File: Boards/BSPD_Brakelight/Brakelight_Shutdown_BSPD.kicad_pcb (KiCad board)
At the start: 2 copper layers, 91.4 x 66 mm, 85 parts, among them IC1 ATMEGA16M1, J2 MM_F_RA_20, J3 CONN_02X03, Q1 SSM3K333R, Q2 SSM3K333R, Q3 SSM3K333R, Q6 SSM3K333R, U1 SN74LVC1G08, U101 TPS560430YF, U2 MCP6001, U3 CAN_Transceiver, U4 MCP6001, U5 SN74LVC1G02, U6 SN74LVC1G02, U7 MCP6001, U8 SN74LVC1G32, Y1 Crystal_SMD

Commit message: Completed BSPD rev 2
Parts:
- moved G*** 128.3 mm to (235.9, 97.8), turned to 180 degrees
- moved R3 116.5 mm to (260.1, 99.5), turned to 270 degrees
- moved C1 103.1 mm to (235.1, 72.8)
- moved R1 100.4 mm to (232.2, 71.8), turned to 90 degrees
- moved C2 100.4 mm to (235.1, 70.7), turned to 0 degrees
- moved R23 94.8 mm to (219.9, 90.6), turned to 270 degrees
- moved IC1 92.7 mm to (233.4, 63.0), turned to 270 degrees
- moved R41 91.7 mm to (226.6, 53.4), turned to 270 degrees
- moved Q3 91.6 mm to (219.8, 94.3)
- moved R22 90.7 mm to (218.8, 97.8), turned to 90 degrees
- moved C9 90.3 mm to (230.5, 50.4), turned to 0 degrees
- moved C4 89.5 mm to (225.1, 57.9)
- moved C3 89.5 mm to (222.1, 60.5)
- moved Y1 89.5 mm to (225.2, 60.7)
- moved D5 89.4 mm to (209.8, 99.4), turned to 90 degrees
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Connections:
- IC1 pad 13: /SHUTDOWN_SENSE_BSPD_PIN -> /BSPD_RELAY_INTENTION
- IC1 pad 14: /DEBUG_LED_1 -> Net-(IC1-Pad14)
- IC1 pad 15: /DEBUG_LED_2 -> Net-(IC1-Pad15)
- IC1 pad 16: /DEBUG_LED_3 -> Net-(IC1-Pad16)
- IC1 pad 25: Net-(IC1-Pad25) -> /SHUTDOWN_SENSE_BSPD_PIN
- IC1 pad 26: Net-(IC1-Pad26) -> /DEBUG_LED_1
- IC1 pad 27: Net-(IC1-Pad27) -> /DEBUG_LED_2
- IC1 pad 28: Net-(IC1-Pad28) -> /DEBUG_LED_3
- IC1 pad 9: /BSPD_RELAY_INTENTION -> Net-(IC1-Pad9)
- R41 pad 2: Net-(IC1-Pad23) -> Net-(IC1-Pad8)
- R42 pad 1: Net-(IC1-Pad24) -> Net-(IC1-Pad9)
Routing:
- net /BRAKE_PRESSURE_SENSE: track 186.0 -> 60.7 mm, vias 10 -> 0
- net VCC: track 404.7 -> 338.2 mm, vias 11 -> 6
- net /BSPD_RELAY_LSD: track 78.1 -> 13.8 mm, vias 4 -> 0
- net /DEBUG_LED_1: track 16.6 -> 70.3 mm
- net /BRAKELIGHT_GATE: track 85.1 -> 33.7 mm, vias 6 -> 2
- net /DEBUG_LED_3: track 21.8 -> 72.3 mm
- net /DEBUG_LED_2: track 19.2 -> 68.5 mm
- net /BRAKELIGHT_LSD: track 138.5 -> 91.9 mm, vias 4 -> 0
- net /MOSI: track 122.1 -> 162.6 mm, vias 2 -> 1
- net /RJ45_LED_O: track 48.1 -> 9.06 mm, vias 2 -> 0
- net /RJ45_LED_G: track 49.0 -> 10.7 mm, vias 2 -> 0
- net /MISO: track 126.3 -> 160.8 mm, vias 2 -> 0
- net /RESET: track 133.0 -> 162.7 mm, vias 4 -> 0
- net GND: track 161.5 -> 138.6 mm, vias 49 -> 45
- net /BSPD_CURRENT_SENSE: track 83.8 -> 105.5 mm, vias 10 -> 0
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- added copper zone on B.Cu, net (none)
- removed copper zone on B.Cu, net GND
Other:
- board size 91.4 x 66 mm -> 76.2 x 67.3 mm
- board text added: "Jack Greenberg - BSPD/Brakelight Rev 2 | 02/03/20 | OEM - MKV"
- board text added: "Jumper"
- board text removed: "12V"
- board text removed: "5V"
- board text removed: "For Instructional Use Only."
- board text removed: "Jack Greenberg BSPD/Brakelight Rev 1 | 12/02/19 OEM - MKV"
- board text removed: "SOLIDWORKS Educational Product."

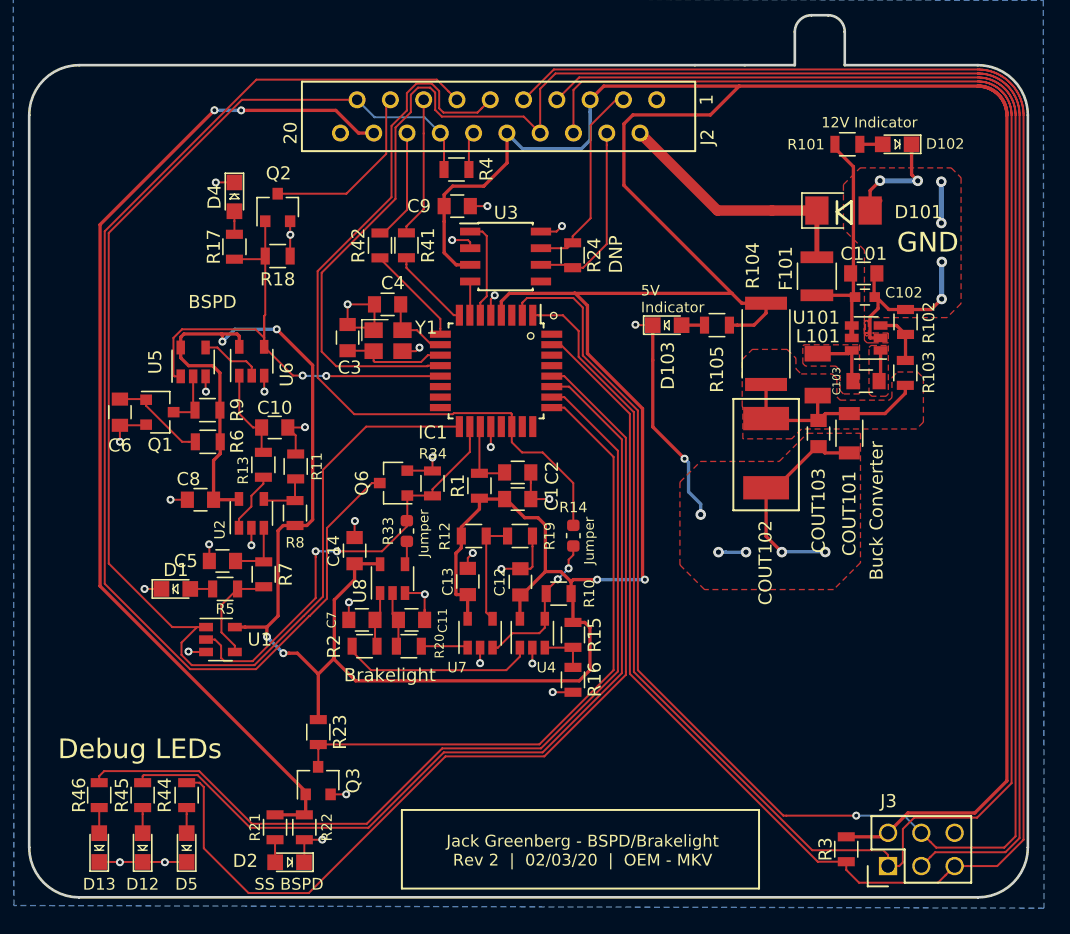
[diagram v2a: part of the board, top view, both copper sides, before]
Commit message: Updated buck on BSPD and added test points
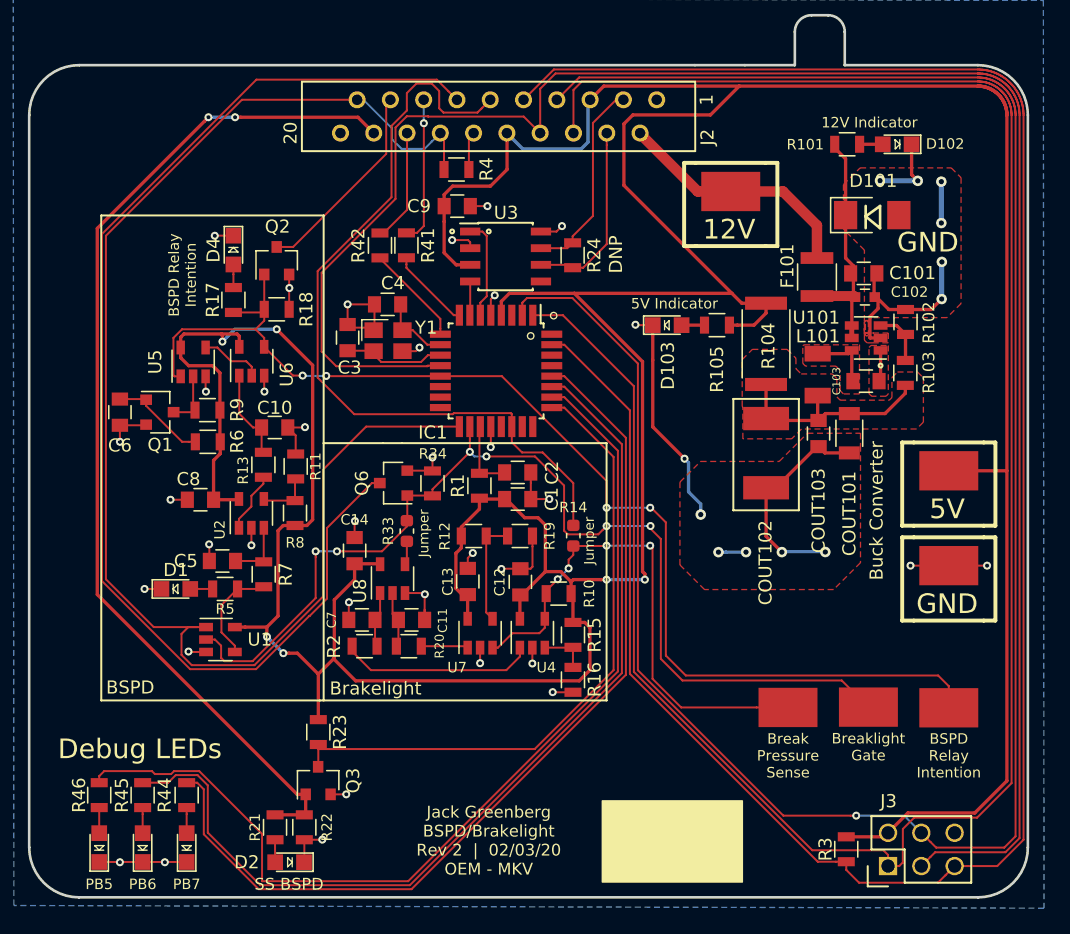
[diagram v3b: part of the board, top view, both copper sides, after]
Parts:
- added TP1: Test_Point_SMD, footprints:Test_Point_SMD, F.Cu at (255.7, 88.7)
- added TP2: Test_Point_SMD, footprints:Test_Point_SMD, F.Cu at (261.8, 88.6)
- added TP3: Test_Point_SMD, footprints:Test_Point_SMD, F.Cu at (268.0, 88.7)
- added TP4: Test_Point_SMD, footprints:Test_Point_SMD, F.Cu at (251.3, 49.3)
- added TP5: Test_Point_SMD, footprints:Test_Point_SMD, F.Cu at (268.0, 70.6)
- added TP6: Test_Point_SMD, footprints:Test_Point_SMD, F.Cu at (268.0, 77.9)
- R101: value R_200 -> R_1K
- moved D4 4.06 mm to (213.4, 53.8)
- moved Q2 4.06 mm to (216.7, 54.6)
- moved R17 4.06 mm to (213.4, 57.6)
- moved R18 4.06 mm to (216.7, 58.3)
- moved D101 2.22 mm to (262.1, 51.1)
- moved F101 0.06 mm to (257.9, 55.8)
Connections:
- D101 pad 1: +12V -> Net-(C101-Pad1)
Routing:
- net /BSPD_RELAY_INTENTION: track 39.7 -> 90.3 mm, vias 2 -> 4
- net /BRAKELIGHT_GATE: track 33.7 -> 80.2 mm, vias 2 -> 6
- net Net-(R10-Pad2): track 11.8 -> 39.9 mm, vias 2 -> 4
- net /DEBUG_LED_1: track 70.3 -> 76.2 mm
- net /DEBUG_LED_2: track 68.5 -> 73.7 mm
- net VCC: track 338.2 -> 342.7 mm
- net /SCK: track 150.1 -> 146.7 mm
- net /BSPD_CURRENT_SENSE: track 105.5 -> 108.4 mm
- net GND: track 138.6 -> 140.6 mm, vias 45 -> 47
- net /BSPD_RELAY_LSD: track 13.8 -> 15.6 mm
- net /DEBUG_LED_3: track 72.3 -> 71.4 mm
- net +12V: track 19.8 -> 18.9 mm
- net /RJ45_LED_G: track 10.7 -> 11.2 mm, vias 0 -> 1
- added copper zone on B.Cu, net GND
- removed copper zone on B.Cu, net (none)
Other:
- board text added: "12V"
- board text added: "5V"
- board text added: "BSPD Relay Intention"
- board text added: "Break Pressure Sense"
- board text added: "Breaklight Gate"
- board text added: "Jack Greenberg BSPD/Brakelight Rev 2 | 02/03/20 OEM - MKV"
- board text added: "PB5"
- board text added: "PB6"
- board text added: "PB7"
- board text removed: "Jack Greenberg - BSPD/Brakelight Rev 2 | 02/03/20 | OEM - MKV"

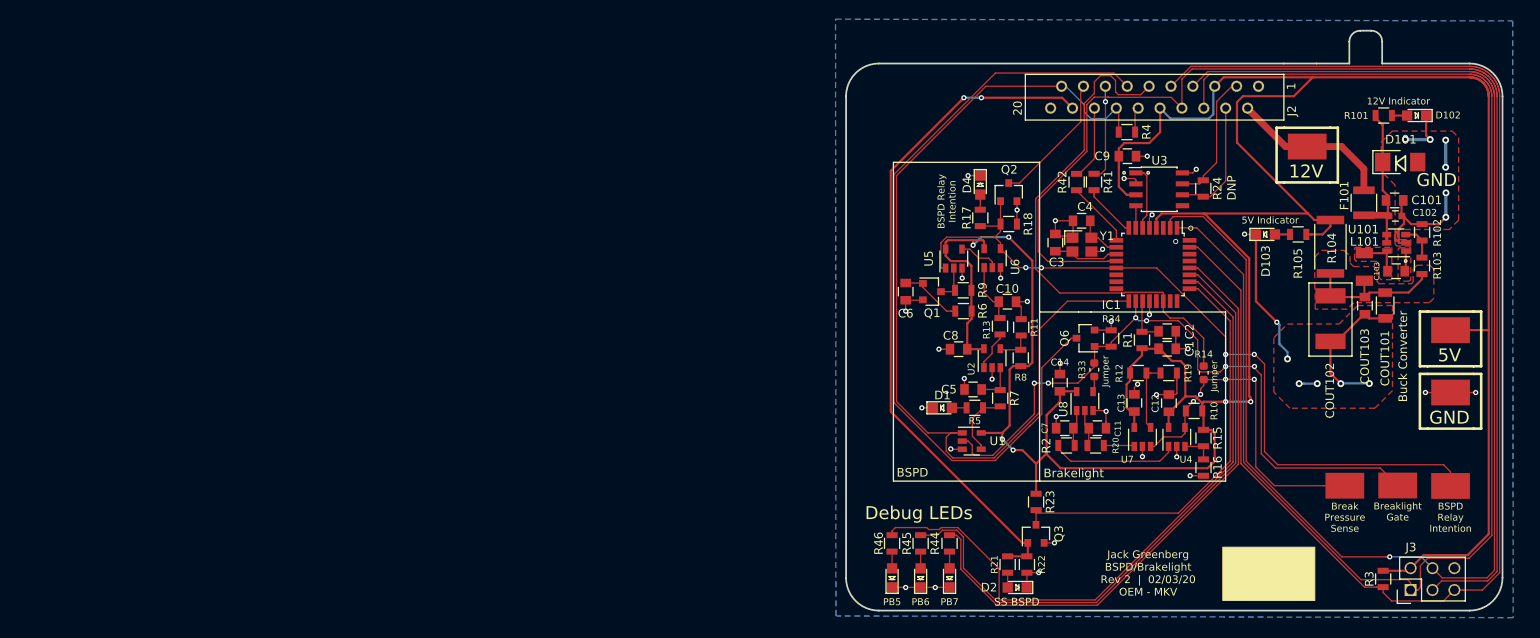
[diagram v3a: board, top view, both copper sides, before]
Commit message: Update BSPD shape
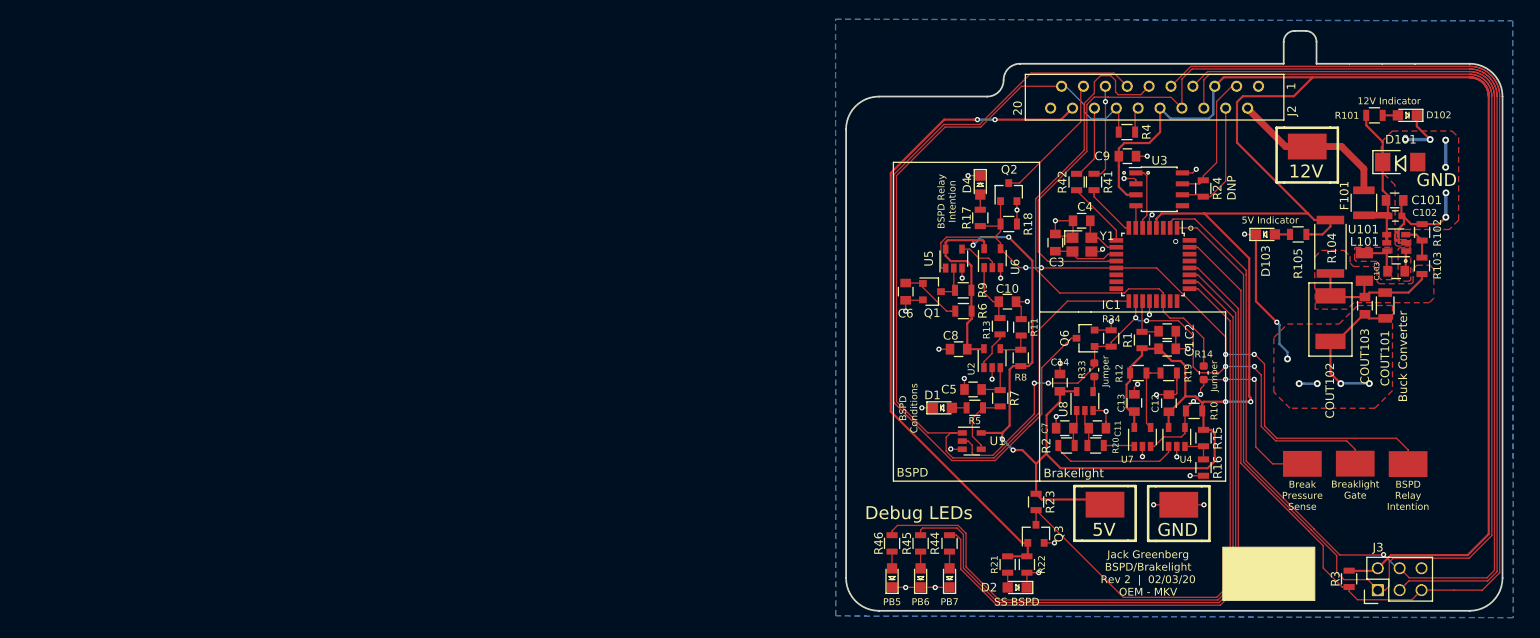
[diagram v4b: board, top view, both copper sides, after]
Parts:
- moved TP5 44.9 mm to (227.9, 90.9)
- moved TP6 34.1 mm to (236.4, 90.9)
- moved TP3 5.54 mm to (263.0, 86.2)
- moved TP1 5.54 mm to (250.8, 86.1)
- moved TP2 5.54 mm to (256.9, 86.1)
- moved R3 3.95 mm to (256.2, 99.5)
- moved J3 3.81 mm to (259.5, 100.8)
- moved D102 1.08 mm to (263.0, 45.7)
- moved R101 1.08 mm to (259.1, 45.7)
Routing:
- net /SHUTDOWN_SENSE_BSPD_PIN: track 49.3 -> 65.9 mm
- net /DEBUG_LED_2: track 73.7 -> 82.8 mm
- net /DEBUG_LED_1: track 76.2 -> 84.8 mm
- net /DEBUG_LED_3: track 71.4 -> 79.7 mm
- net Net-(R10-Pad2): track 39.9 -> 31.8 mm
- net VCC: track 342.7 -> 350.7 mm
- net /BSPD_RELAY_INTENTION: track 90.3 -> 82.5 mm
- net /BRAKELIGHT_GATE: track 80.2 -> 73.5 mm
- net /SCK: track 146.7 -> 150.5 mm
- net /RESET: track 162.9 -> 164.2 mm
- net /SHUTDOWN_SENSE_BSPD: track 79.2 -> 78.2 mm
- net /MOSI: track 162.6 -> 161.5 mm
- net /MISO: track 160.8 -> 161.6 mm
- net Net-(C101-Pad1): track 18.4 -> 19.2 mm
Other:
- outline, holes or cut-outs redrawn
- board text added: "BSPD Conditions"

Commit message: Fixed shape of BSPD board
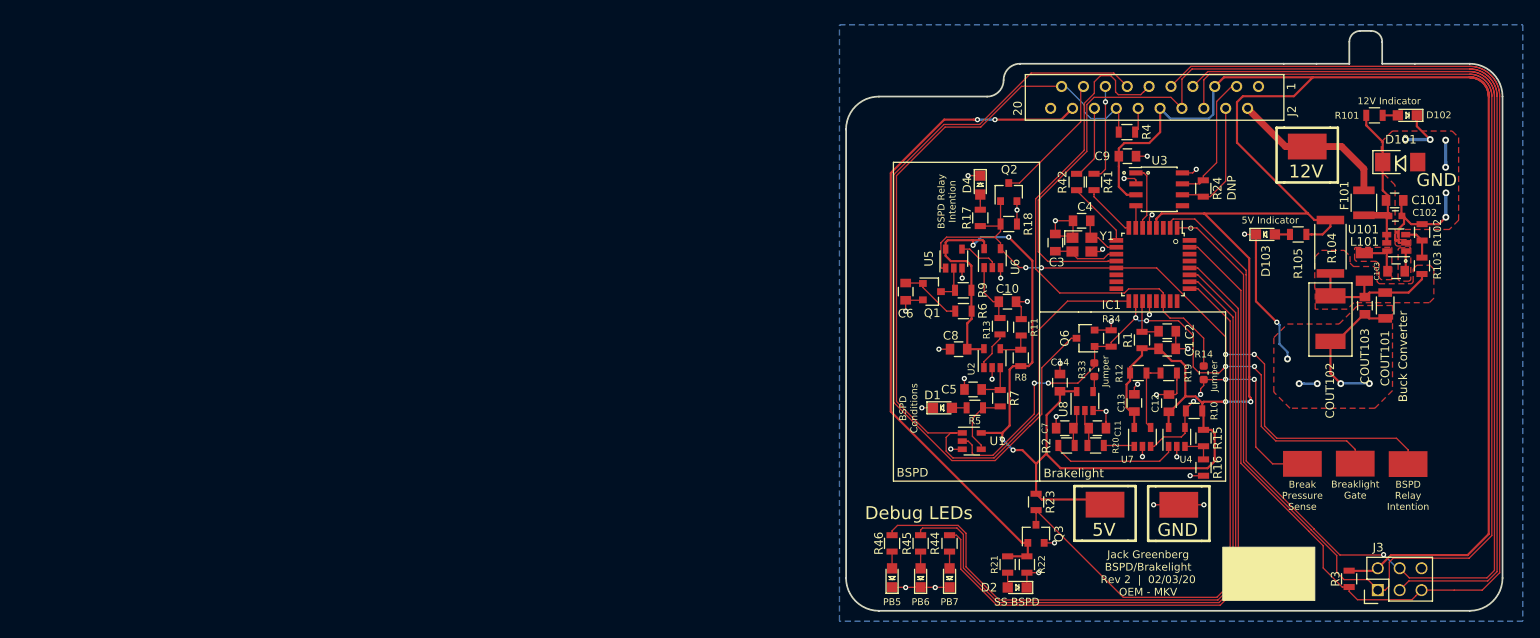
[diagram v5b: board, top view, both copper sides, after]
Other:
- outline, holes or cut-outs redrawn

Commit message: Final tweaks and generated pdfs
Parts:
- moved R24 0.19 mm to (239.3, 54.4)
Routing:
- net /CAN_HIGH: track 15.4 -> 16.1 mm
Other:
- board text removed: "Buck Converter"
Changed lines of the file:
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@@
   (general
     (thickness 1.6)
-    (drawings 82)
+    (drawings 80)
     (tracks 1060)
     (zones 0)
@@
   )
   (module footprints:R_0805_OEM (layer F.Cu)
-    (at 239.268 54.168 270)
+    (at 239.268 54.356 270)
     (descr "Resistor SMD 0805, reflow soldering, Vishay (see dcrcw.pdf)")
     (tags "resistor 0805")
@@
   (gr_line (start 252.4125 39.687499) (end 256.2225 39.687499) (layer Edge.Cuts) (width 0.2))
   (gr_line (start 260.032501 39.687499) (end 263.8425 39.687499) (layer Edge.Cuts) (width 0.2))
-  (gr_line (start 266.382501 103.187499) (end 266.382501 39.687499) (layer Dwgs.User) (width 0.2))
   (gr_arc (start 270.192501 43.4975) (end 274.002501 43.4975) (angle -90) (layer Edge.Cuts) (width 0.2))
   (gr_arc (start 270.192501 99.377499) (end 270.192501 103.187499) (angle -90) (layer Edge.Cuts) (width 0.2))
@@
     (effects (font (size 1.5 1.5) (thickness 0.2)))
   )
-  (gr_text "Buck Converter" (at 262.4582 73.66 90) (layer F.SilkS)
-    (effects (font (size 1 1) (thickness 0.15)))
-  )
   (gr_text GND (at 266.3698 53.1876) (layer F.SilkS)
     (effects (font (size 1.5 1.5) (thickness 0.3)))
@@
   (segment (start 240.6015 42.32656) (end 240.6015 42.3037) (width 0.254) (layer B.Cu) (net 2))
   (segment (start 240.4364 42.49166) (end 240.6015 42.32656) (width 0.254) (layer B.Cu) (net 2))
-  (segment (start 240.4364 45.5422) (end 240.4364 42.49166) (width 0.254) (layer B.Cu) (net 2))
-  (segment (start 239.9284 46.0502) (end 240.4364 45.5422) (width 0.254) (layer B.Cu) (net 2))
-  (segment (start 234.2515 44.86656) (end 235.43514 46.0502) (width 0.254) (layer B.Cu) (net 2))
-  (segment (start 235.43514 46.0502) (end 239.9284 46.0502) (width 0.254) (layer B.Cu) (net 2))
+  (segment (start 240.46179 42.46627) (end 240.6015 42.32656) (width 0.254) (layer F.Cu) (net 2))
+  (segment (start 239.7125 46.228) (end 240.46179 45.47871) (width 0.254) (layer F.Cu) (net 2))
+  (segment (start 234.2515 44.86656) (end 235.61294 46.228) (width 0.254) (layer F.Cu) (net 2))
+  (segment (start 240.46179 45.47871) (end 240.46179 42.46627) (width 0.254) (layer F.Cu) (net 2))
+  (segment (start 235.61294 46.228) (end 239.7125 46.228) (width 0.254) (layer F.Cu) (net 2))
   (segment (start 259.5245 100.7237) (end 259.5245 100.7872) (width 0.1524) (layer F.Cu) (net 3))
   (segment (start 254.762 98.706541) (end 255.623459 99.568) (width 0.1524) (layer F.Cu) (net 3))
@@
   (segment (start 238.77524 75.55992) (end 241.12728 75.55992) (width 0.1524) (layer F.Cu) (net 53))
   (segment (start 241.12728 75.55992) (end 241.554001 75.133199) (width 0.1524) (layer F.Cu) (net 53))
-  (segment (start 238.857084 53.628916) (end 239.268 53.218) (width 0.1524) (layer F.Cu) (net 54))
-  (segment (start 236.850784 53.628916) (end 238.857084 53.628916) (width 0.1524) (layer F.Cu) (net 54))
-  (segment (start 243.11864 42.32656) (end 243.1415 42.3037) (width 0.1524) (layer F.Cu) (net 54))
-  (segment (start 242.55984 42.32656) (end 243.11864 42.32656) (width 0.1524) (layer F.Cu) (net 54))
-  (segment (start 240.8174 44.069) (end 242.55984 42.32656) (width 0.1524) (layer F.Cu) (net 54))
-  (segment (start 240.8174 51.1662) (end 240.8174 44.069) (width 0.1524) (layer F.Cu) (net 54))
-  (segment (start 239.268 53.218) (end 239.268 52.7156) (width 0.1524) (layer F.Cu) (net 54))
-  (segment (start 239.268 52.7156) (end 240.8174 51.1662) (width 0.1524) (layer F.Cu) (net 54))
-  (segment (start 239.048916 54.898916) (end 239.268 55.118) (width 0.1524) (layer F.Cu) (net 55))
-  (segment (start 236.850784 54.898916) (end 239.048916 54.898916) (width 0.1524) (layer F.Cu) (net 55))
-  (segment (start 241.8715 53.3169) (end 241.8715 44.86656) (width 0.1524) (layer F.Cu) (net 55))
-  (segment (start 239.268 55.118) (end 240.0704 55.118) (width 0.1524) (layer F.Cu) (net 55))
-  (segment (start 240.0704 55.118) (end 241.8715 53.3169) (width 0.1524) (layer F.Cu) (net 55))
+  (segment (start 239.045084 53.628916) (end 239.268 53.406) (width 0.1524) (layer F.Cu) (net 54))
+  (segment (start 236.850784 53.628916) (end 239.045084 53.628916) (width 0.1524) (layer F.Cu) (net 54))
+  (segment (start 242.47094 42.32656) (end 243.1415 42.32656) (width 0.1524) (layer F.Cu) (net 54))
+  (segment (start 240.8555 43.942) (end 242.47094 42.32656) (width 0.1524) (layer F.Cu) (net 54))
+  (segment (start 240.8555 52.6209) (end 240.8555 43.942) (width 0.1524) (layer F.Cu) (net 54))
+  (segment (start 239.268 53.406) (end 240.0704 53.406) (width 0.1524) (layer F.Cu) (net 54))
+  (segment (start 240.0704 53.406) (end 240.8555 52.6209) (width 0.1524) (layer F.Cu) (net 54))
+  (segment (start 238.860916 54.898916) (end 239.268 55.306) (width 0.1524) (layer F.Cu) (net 55))
+  (segment (start 236.850784 54.898916) (end 238.860916 54.898916) (width 0.1524) (layer F.Cu) (net 55))
+  (segment (start 240.0704 55.306) (end 239.268 55.306) (width 0.1524) (layer F.Cu) (net 55))
+  (segment (start 241.8715 53.5049) (end 240.0704 55.306) (width 0.1524) (layer F.Cu) (net 55))
+  (segment (start 241.8715 44.86656) (end 241.8715 53.5049) (width 0.1524) (layer F.Cu) (net 55))
   (segment (start 223.9504 71.5518) (end 224.5528 71.5518) (width 0.1524) (layer F.Cu) (net 56))
   (segment (start 220.52281 74.97939) (end 223.9504 71.5518) (width 0.1524) (layer F.Cu) (net 56))
